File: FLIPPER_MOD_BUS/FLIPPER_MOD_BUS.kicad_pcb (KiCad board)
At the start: 2 copper layers, 62.8 x 23.2 mm, 21 parts, among them J1 Conn_01x02, J2 Conn_01x10_Socket, J3 Conn_01x08_Socket, U1 SP3485EN

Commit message: UPDATE FLIPPER MODBUS SHIELD
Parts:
- moved kibuzzard-65A7F695 5.08 mm to (150.2, 88.6)
- moved kibuzzard-65A7F6E6 2.54 mm to (152.7, 88.6)
- moved kibuzzard-65A7F6FE 2.54 mm to (155.2, 88.6)
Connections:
- J2 pad 4: /TX -> unconnected-(J2-Pin_4-Pad4)
- J2 pad 6: /DE -> /TX
- J2 pad 7: /RE -> /DE
- J2 pad 8: unconnected-(J2-Pin_8-Pad8) -> /RE
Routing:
- net /TX: track 13.3 -> 18.1 mm, vias 0 -> 1
- net /DE: track 21.6 -> 24.1 mm
- net /RE: track 25.7 -> 28.1 mm
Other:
- board text added: "A"
- board text added: "B"
- board text added: "MOD_BUS V1.0"
- board text removed: "MOD_BUS"

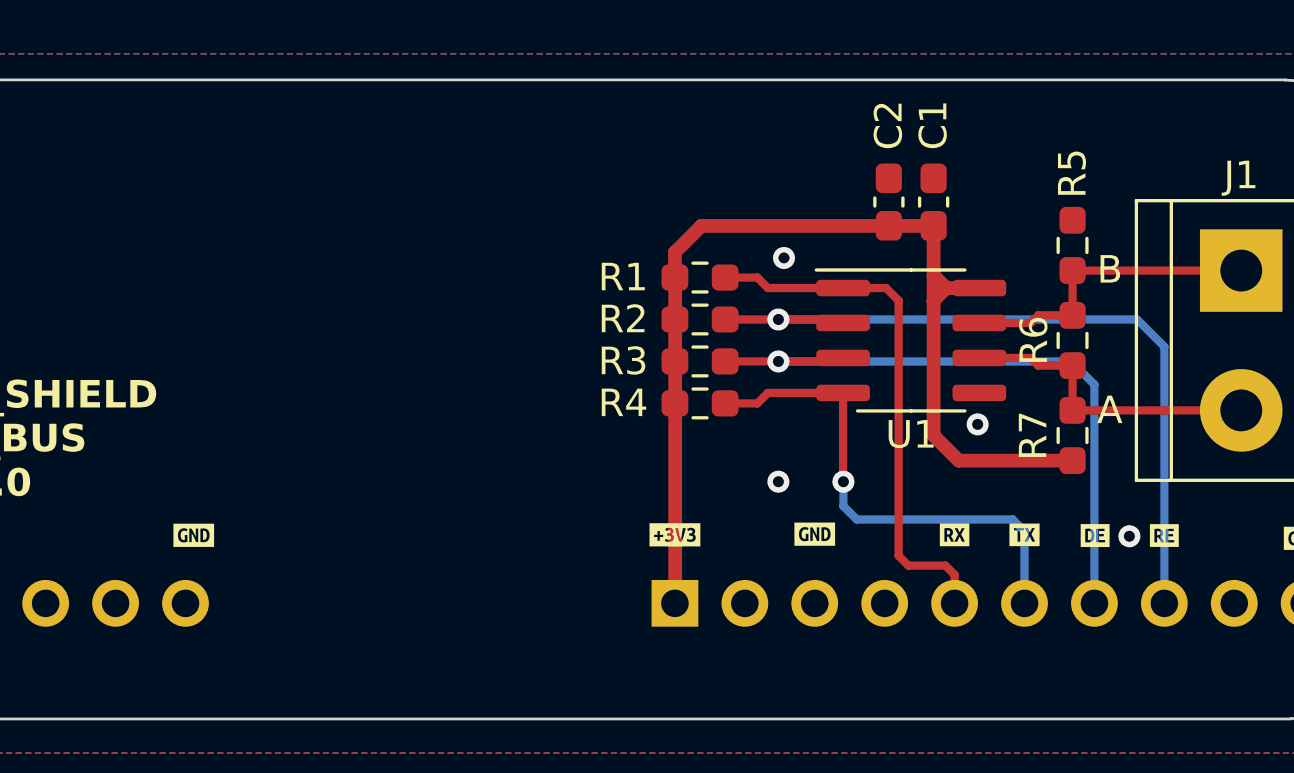
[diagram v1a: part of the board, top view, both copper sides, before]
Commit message: Flipper_MOD_BUS RX TX Fixed
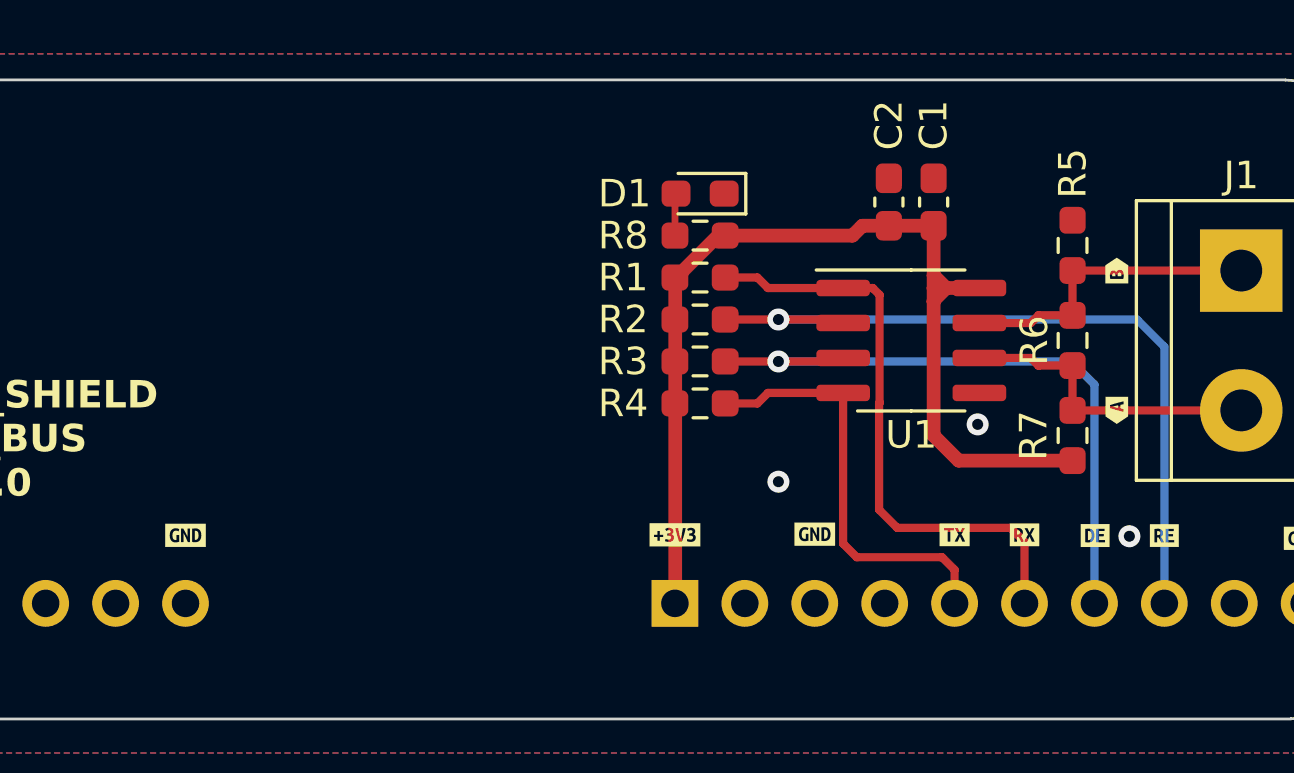
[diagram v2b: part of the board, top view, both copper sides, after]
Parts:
- added D1: LED_Small, LED_SMD:LED_0603_1608Metric_Pad1.05x0.95mm_HandSolder, F.Cu at (138.4, 76.2)
- added R8: 1K, Resistor_SMD:R_0603_1608Metric_Pad0.98x0.95mm_HandSolder, F.Cu at (138.4, 77.7)
- added kibuzzard-65A85C7A: G***, kibuzzard-65A85C7A, F.Cu at (153.5, 84.1)
- added kibuzzard-65A85CB8: G***, kibuzzard-65A85CB8, F.Cu at (153.5, 79.0)
- moved kibuzzard-65A7F695 2.54 mm to (147.6, 88.6)
- moved kibuzzard-65A7F6B7 2.54 mm to (150.2, 88.6)
- moved kibuzzard-644AD5FD 0.30 mm to (119.7, 88.6)
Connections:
- J2 pad 5: /RX -> /TX
- J2 pad 6: /TX -> /RX
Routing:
- net /TX: track 18.1 -> 15.6 mm, vias 1 -> 0
- net /RX: track 19.3 -> 21.7 mm
- net Net-(D1-A): track 0.00 -> 1.54 mm
- net +3V3: track 38.6 -> 38.1 mm
- net GND: vias 4 -> 3
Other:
- board text removed: "A"
- board text removed: "B"

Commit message: Flipper Mod Bus Silkcscreen Updated
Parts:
- removed D1: LED_Small, LED_SMD:LED_0603_1608Metric_Pad1.05x0.95mm_HandSolder
- removed R8: 1K, Resistor_SMD:R_0603_1608Metric_Pad0.98x0.95mm_HandSolder
- removed kibuzzard-65A85C7A: G***, kibuzzard-65A85C7A
- removed kibuzzard-65A85CB8: G***, kibuzzard-65A85CB8
- added G***: LOGO, Aesthetics:electronic_cats_logo_8x6, F.Cu at (110.8, 78.4)
- added REF**: OSHW-Logo_5.7x6mm_SilkScreen, Symbol:OSHW-Logo_5.7x6mm_SilkScreen, F.Cu at (128.8, 91.1)
- added kibuzzard-65B028C6: G***, kibuzzard-65B028C6, F.Cu at (153.3, 84.1)
- added kibuzzard-65B028F3: G***, kibuzzard-65B028F3, F.Cu at (153.3, 79.0)
- moved C1 1.62 mm to (145.8, 77.7), turned to 0 degrees
- moved C2 0.69 mm to (145.8, 76.1), turned to 0 degrees
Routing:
- net Net-(D1-A): track 1.54 -> 0.00 mm
- net +3V3: track 38.1 -> 39.4 mm
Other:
- board text added: "FLIPPER SHIELD MODBUS V1.0"
- board text removed: "FLIPPER_SHIELD"
- board text removed: "MOD_BUS V1.0"

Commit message: Flipper MODBUS Back Silkscreen Updated
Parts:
- added G***: LOGO, Aesthetics:electronic_cats_logo_8x6, B.Cu at (130.6, 78.8)

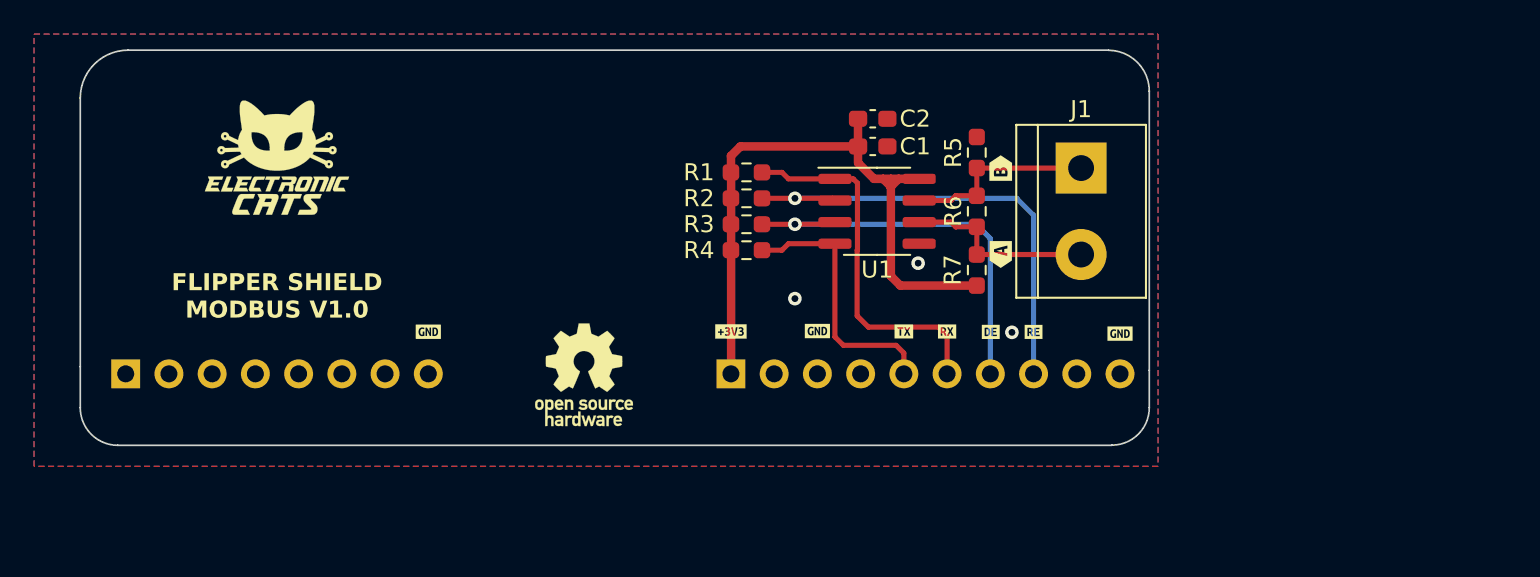
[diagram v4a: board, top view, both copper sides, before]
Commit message: Flipper MODBUS Headers Updated
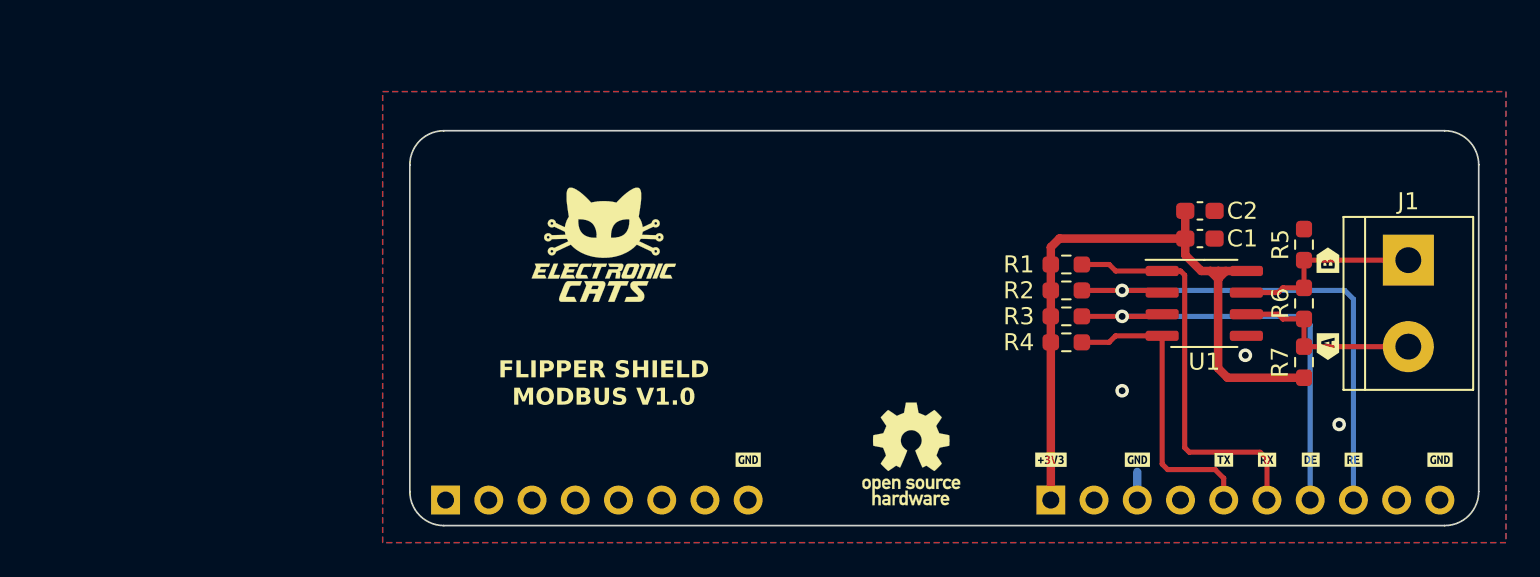
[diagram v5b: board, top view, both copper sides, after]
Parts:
- J2: footprint Connector_PinHeader_2.54mm:PinHeader_1x10_P2.54mm_Horizontal -> Connector_PinHeader_2.54mm:PinHeader_1x10_P2.54mm_Vertical
- J3: footprint Connector_PinHeader_2.54mm:PinHeader_1x08_P2.54mm_Horizontal -> Connector_PinHeader_2.54mm:PinHeader_1x08_P2.54mm_Vertical
- moved kibuzzard-65A7F66D 20.3 mm to (161.3, 96.1)
- moved kibuzzard-65A7F651 20.3 mm to (156.3, 96.1)
- moved kibuzzard-65A7F695 20.3 mm to (166.4, 96.1)
- moved kibuzzard-65A7F6B7 20.3 mm to (169.0, 96.1)
- moved kibuzzard-65A7F6E6 20.2 mm to (171.5, 96.1)
- moved kibuzzard-65A7F6FE 20.2 mm to (174.0, 96.1)
- moved kibuzzard-644AD5FD 20.2 mm to (138.5, 96.1)
- moved kibuzzard-65A7F66D 20.2 mm to (179.1, 96.1)
- moved J2 20.2 mm to (156.3, 98.5)
- moved J3 20.2 mm to (120.7, 98.5)
- moved C2 20.0 mm to (165.0, 81.5)
- moved J1 20.0 mm to (177.3, 84.4)
- moved kibuzzard-65B028C6 20.0 mm to (172.5, 89.5)
- moved kibuzzard-65B028F3 20.0 mm to (172.5, 84.4)
- moved C1 20.0 mm to (165.0, 83.1)
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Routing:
- net +3V3: track 39.4 -> 41.9 mm
- net /RE: track 28.1 -> 29.9 mm
- net /RX: track 21.7 -> 23.5 mm
- net /DE: track 24.1 -> 25.9 mm
- net GND: track 0.00 -> 1.65 mm
- net /TX: track 15.6 -> 17.2 mm
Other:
- outline, holes or cut-outs redrawn

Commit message: fix(hw): DE RE Pull Down & Jumper
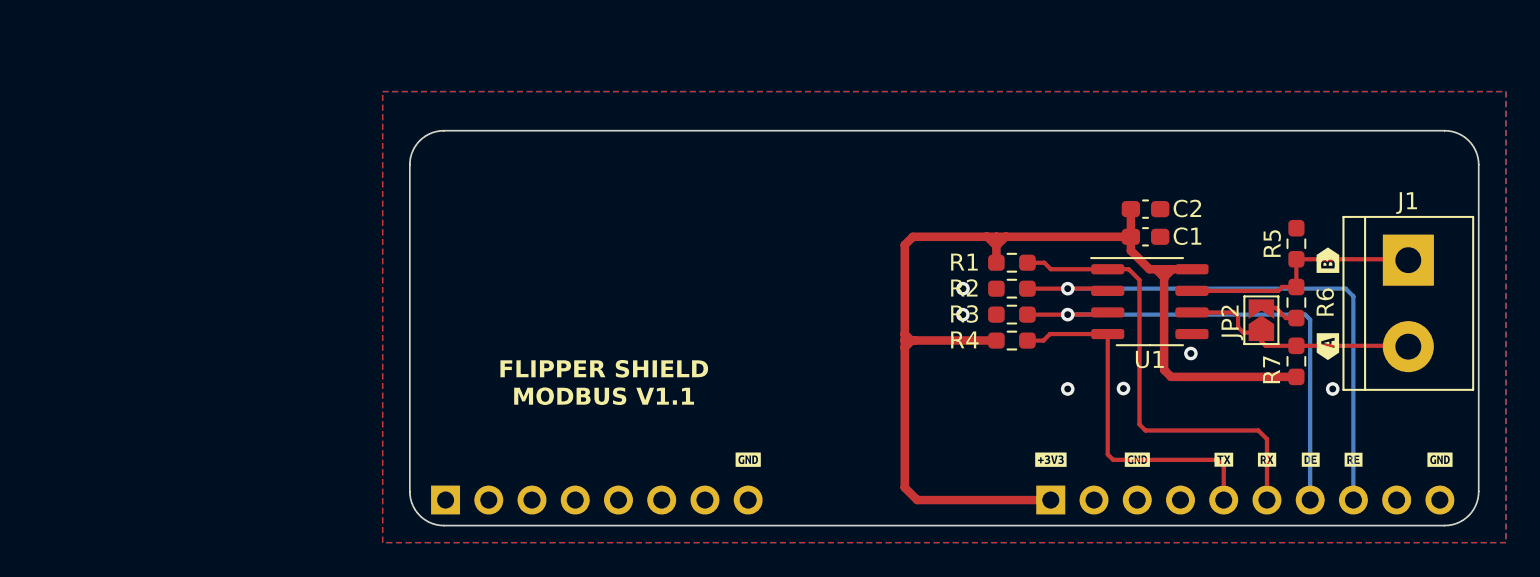
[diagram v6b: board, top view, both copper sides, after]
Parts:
- removed G*** (x2): LOGO, Aesthetics:electronic_cats_logo_8x6
- removed REF**: OSHW-Logo_5.7x6mm_SilkScreen, Symbol:OSHW-Logo_5.7x6mm_SilkScreen
- added JP2: Jumper, Jumper:SolderJumper-2_P1.3mm_Open_TrianglePad1.0x1.5mm, F.Cu at (168.6, 87.9)
- moved C1 3.20 mm to (161.8, 83.0)
- moved C2 3.20 mm to (161.8, 81.4)
- moved R1 3.20 mm to (154.0, 84.6)
- moved R2 3.20 mm to (154.0, 86.1)
- moved R3 3.20 mm to (154.0, 87.6)
- moved R4 3.20 mm to (154.0, 89.1)
- moved U1 3.20 mm to (162.1, 86.8)
- moved R5 0.45 mm to (170.7, 83.4)
- moved R6 0.45 mm to (170.7, 86.9)
- moved R7 0.45 mm to (170.7, 90.3)
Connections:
- R2 pad 1: +3V3 -> GND
- R3 pad 1: +3V3 -> GND
- R6 pad 2: /RS485A -> Net-(JP2-B)
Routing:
- net +3V3: track 41.9 -> 68.4 mm
- net /DE: track 25.9 -> 29.7 mm
- net /TX: track 17.2 -> 21.0 mm
- net /RE: track 29.9 -> 33.7 mm
- net /RS485B: track 11.3 -> 14.8 mm
- net /RX: track 23.5 -> 26.9 mm
- net /RS485A: track 11.3 -> 14.2 mm
- net Net-(JP2-B): track 0.00 -> 2.31 mm
- net GND: track 1.65 -> 0.00 mm, vias 3 -> 6
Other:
- board text added: "FLIPPER SHIELD MODBUS V1.1"

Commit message: feat(hw): add logo
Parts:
- added G***: LOGO, Aesthetics:electronic_cats_logo_8x6, F.Cu at (130.2, 84.6)
- added G***: LOGO, Aesthetics:electronic_cats_logo_8x6, B.Cu at (150.1, 83.6)

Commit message: fix(hw): Jumpers & version Updated
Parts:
- removed JP2: Jumper, Jumper:SolderJumper-2_P1.3mm_Open_TrianglePad1.0x1.5mm
- added J4: Conn_01x02_Socket, Connector_PinHeader_2.54mm:PinHeader_1x02_P2.54mm_Vertical, F.Cu at (167.9, 89.9)
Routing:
- net /RE: track 33.7 -> 39.4 mm
- net /DE: track 29.7 -> 33.8 mm
- net GND: track 0.00 -> 2.73 mm
- net /RS485A: track 14.2 -> 15.0 mm
- net Net-(J4-Pin_2): track 2.31 -> 2.95 mm
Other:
- board text removed: "FLIPPER SHIELD MODBUS V1.0"
